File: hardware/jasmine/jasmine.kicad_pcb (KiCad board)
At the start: 4 copper layers, 70.7 x 53.3 mm, 25 parts, among them J1 NEIGHBOR1, J2 NEIGHBOR2, J3 USB-MICRO-B-SHIELDED, J4 LIPO_BATT_CONN, J7 BONUS_ROW, P1 TEST_POINT, P2 TEST_POINT, P3 TEST_POINT, P4 TEST_POINT, P5 3.7_VDC, U1 MCP73831T

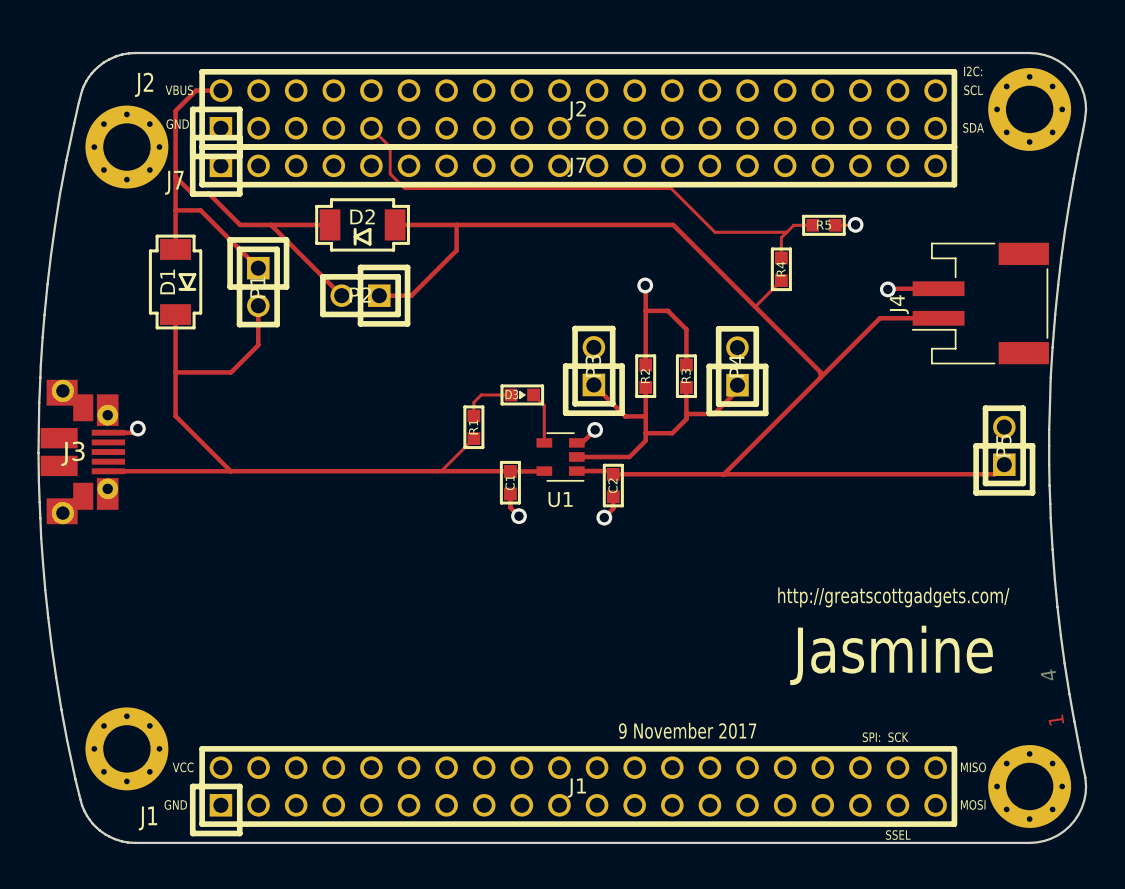
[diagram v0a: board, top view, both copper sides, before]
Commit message: Turned Jasmine into 2-layer board. Re-routes, fixes.
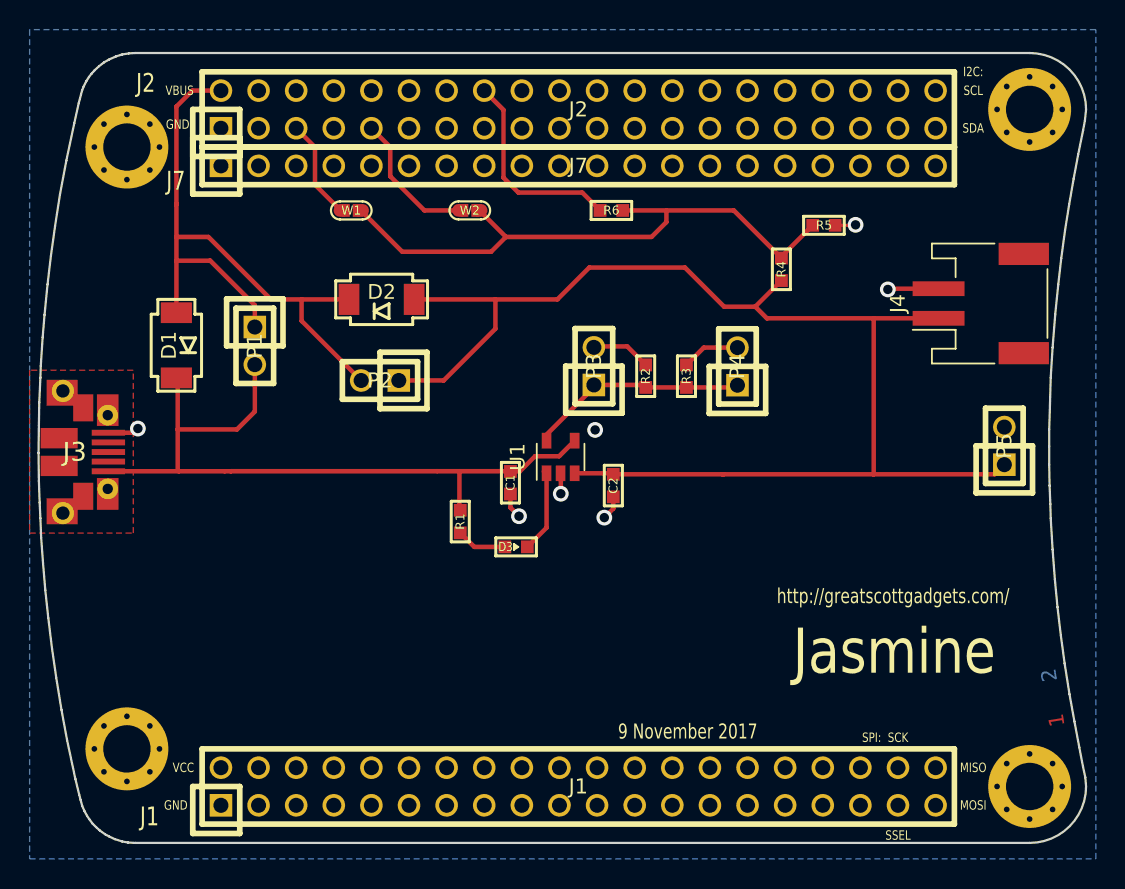
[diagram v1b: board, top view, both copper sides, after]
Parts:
- added R6: 0, gsg-modules:0603, F.Cu at (148.3, 79.2)
- added W1: TEST, gsg-modules:0603-JUMPER, F.Cu at (130.7, 79.2)
- added W2: TEST, gsg-modules:0603-JUMPER, F.Cu at (138.7, 79.2)
- moved D3 10.3 mm to (141.8, 101.9)
- moved R1 6.44 mm to (138.1, 100.2), turned to 270 degrees
- moved P2 5.88 mm to (132.7, 90.7)
- moved D2 5.19 mm to (132.8, 85.2)
- moved D1 4.27 mm to (118.9, 88.3)
- moved P1 3.98 mm to (124.2, 88.4)
- turned U1 to 90 degrees
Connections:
- J1 pad 2: VCC -> Net-(J1-Pad2)
- J3 pad 0: GND -> Net-(J3-Pad0)
- J7 pad 20: VCC -> Net-(J7-Pad20)
- R4 pad 2: /P4_3 -> Net-(R4-Pad2)
- R5 pad 1: /P4_3 -> Net-(R4-Pad2)
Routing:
- net Net-(R4-Pad2): track 0.00 -> 41.1 mm
- net /P4_3: track 35.9 -> 9.45 mm
- net /P7_7: track 0.00 -> 13.9 mm
- net Net-(P3-Pad1): track 22.9 -> 14.9 mm
- net /+5V: track 38.7 -> 46.0 mm
- net /ADC0_0: track 0.00 -> 6.92 mm
- net Net-(C1-Pad2): track 54.0 -> 50.6 mm
- net GND: track 22.9 -> 19.6 mm, vias 7 -> 6
- net Net-(D3-Pad1): track 3.54 -> 5.56 mm
- net Net-(C2-Pad2): track 92.1 -> 90.5 mm
- net (no net): vias 0 -> 1
- added copper zone on B.Cu, net GND
- added copper zone on F.Cu, net Net-(J3-Pad0)
- removed copper zone on C2.Cu, net GND
- removed copper zone on C3.Cu, net VCC
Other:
- copper layers 4 -> 2
- board text removed: "3"
- board text removed: "4"
